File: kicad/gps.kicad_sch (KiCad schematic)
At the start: 4 parts, among them J7 Conn_Coaxial_Small, Q2 IRF540N, U1 NEO-M8N

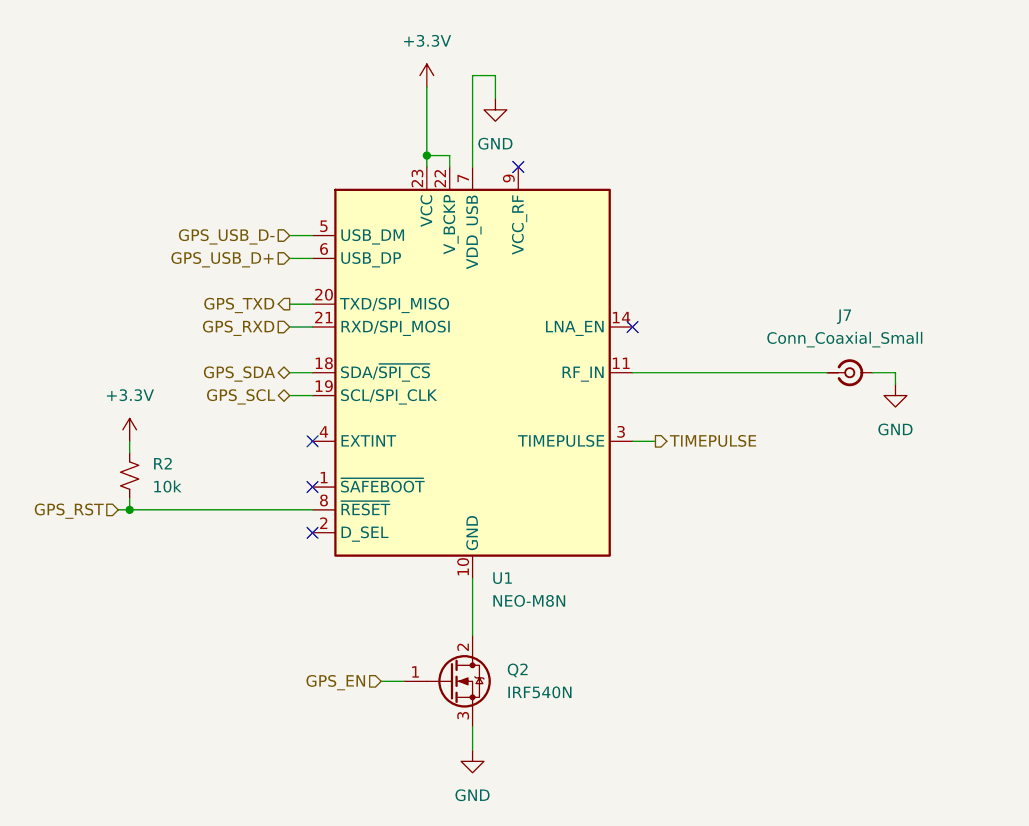
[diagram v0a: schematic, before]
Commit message: make bom cheaper
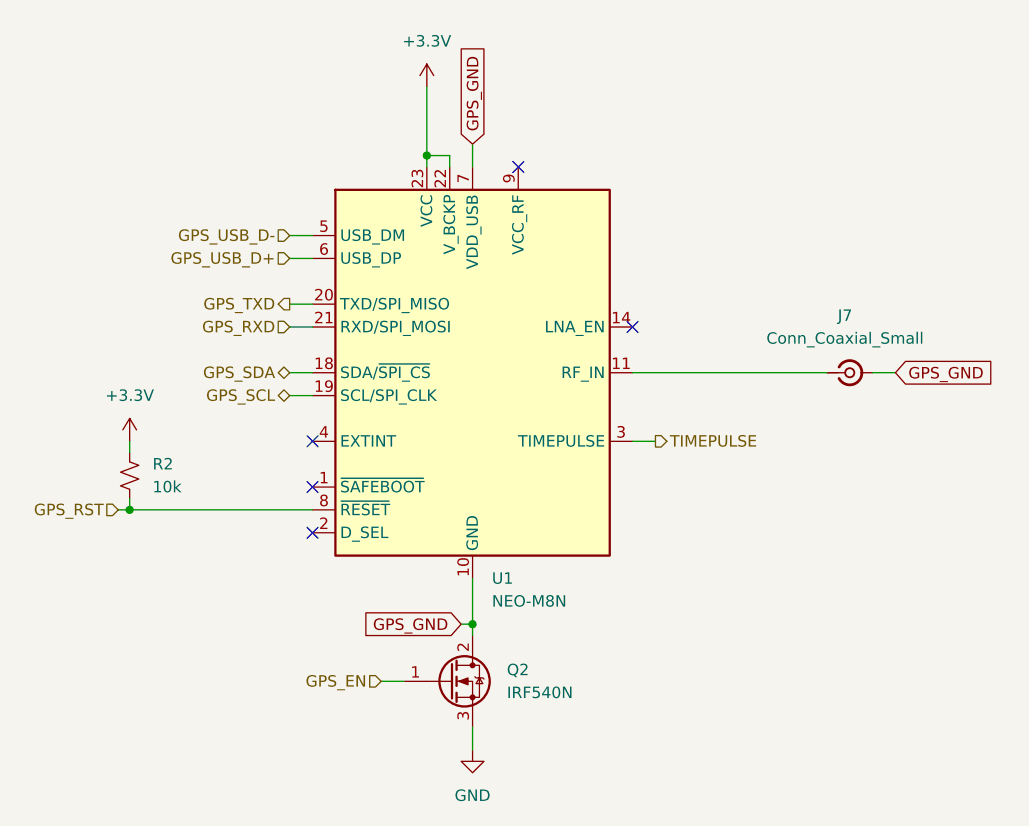
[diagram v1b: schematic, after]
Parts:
- R2: footprint Resistor_THT:R_Axial_DIN0207_L6.3mm_D2.5mm_P10.16mm_Horizontal -> Resistor_THT:R_Axial_DIN0204_L3.6mm_D1.6mm_P2.54mm_Vertical
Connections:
- net GND: no longer J7.2 (Ext), U1.7 (VDD_USB)
- net GPS_GND: now reaches Q2.2 (D), U1.10 (GND), U1.12 (GND), U1.13 (GND), U1.24 (GND)
- net GPS_GND: now also J7.2 (Ext), U1.7 (VDD_USB)
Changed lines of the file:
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@@
+		(color 0 0 0 0)
+	)
+	(junction
+		(at 118.11 124.46)
+		(diameter 0)
 		(color 0 0 0 0)
 	)
@@
 	(wire
 		(pts
+			(xy 118.11 124.46) (xy 118.11 125.73)
+		)
+		(stroke
+			(width 0)
+			(type default)
+		)
+	)
+	(wire
+		(pts
 			(xy 97.79 81.28) (xy 100.33 81.28)
 		)
@@
 	(wire
 		(pts
-			(xy 118.11 119.38) (xy 118.11 125.73)
-		)
-		(stroke
-			(width 0)
-			(type default)
-		)
-	)
-	(wire
-		(pts
 			(xy 78.74 111.76) (xy 80.01 111.76)
 		)
@@
 	(wire
 		(pts
-			(xy 118.11 63.5) (xy 120.65 63.5)
+			(xy 116.84 124.46) (xy 118.11 124.46)
 		)
 		(stroke
@@
 	(wire
 		(pts
-			(xy 118.11 73.66) (xy 118.11 63.5)
-		)
-		(stroke
-			(width 0)
-			(type default)
-		)
-	)
-	(wire
-		(pts
 			(xy 97.79 91.44) (xy 100.33 91.44)
 		)
@@
 	(wire
 		(pts
+			(xy 118.11 119.38) (xy 118.11 124.46)
+		)
+		(stroke
+			(width 0)
+			(type default)
+		)
+	)
+	(wire
+		(pts
 			(xy 113.03 72.39) (xy 113.03 73.66)
 		)
@@
 	(wire
 		(pts
-			(xy 120.65 63.5) (xy 120.65 66.04)
+			(xy 118.11 71.12) (xy 118.11 73.66)
 		)
 		(stroke
@@
 		)
 	)
-	(wire
-		(pts
-			(xy 165.1 97.79) (xy 165.1 96.52)
-		)
-		(stroke
-			(width 0)
-			(type default)
+	(global_label "GPS_GND"
+		(shape input)
+		(at 118.11 71.12 90)
+		(fields_autoplaced yes)
+		(effects
+			(font
+				(size 1.27 1.27)
+			)
+			(justify left)
+		)
+		(property "Intersheetrefs" "${INTERSHEET_REFS}"
+			(at 118.11 59.5472 90)
+			(effects
+				(font
+					(size 1.27 1.27)
+				)
+				(justify left)
+				(hide yes)
+			)
+		)
+	)
+	(global_label "GPS_GND"
+		(shape input)
+		(at 116.84 124.46 180)
+		(fields_autoplaced yes)
+		(effects
+			(font
+				(size 1.27 1.27)
+			)
+			(justify right)
+		)
+		(property "Intersheetrefs" "${INTERSHEET_REFS}"
+			(at 105.2672 124.46 0)
+			(effects
+				(font
+					(size 1.27 1.27)
+				)
+				(justify right)
+				(hide yes)
+			)
+		)
+	)
+	(global_label "GPS_GND"
+		(shape input)
+		(at 165.1 96.52 0)
+		(fields_autoplaced yes)
+		(effects
+			(font
+				(size 1.27 1.27)
+			)
+			(justify left)
+		)
+		(property "Intersheetrefs" "${INTERSHEET_REFS}"
+			(at 176.6728 96.52 0)
+			(effects
+				(font
+					(size 1.27 1.27)
+				)
+				(justify left)
+				(hide yes)
+			)
 		)
 	)
@@
 			)
 		)
-		(property "Footprint" "Resistor_THT:R_Axial_DIN0207_L6.3mm_D2.5mm_P10.16mm_Horizontal"
+		(property "Footprint" "Resistor_THT:R_Axial_DIN0204_L3.6mm_D1.6mm_P2.54mm_Vertical"
 			(at 80.01 107.95 0)
 			(effects
@@
 					(unit 1)
 				)
-			)
-		)
-	)
-	(symbol
-		(lib_id "power:GND")
-		(at 120.65 66.04 0)
-		(unit 1)
-		(exclude_from_sim no)
-		(in_bom yes)
-		(on_board yes)
-		(dnp no)
-		(fields_autoplaced yes)
-		(property "Reference" "#PWR037"
-			(at 120.65 72.39 0)
-			(effects
-				(font
-					(size 1.27 1.27)
-				)
-				(hide yes)
-			)
-		)
-		(property "Value" "GND"
-			(at 120.65 71.12 0)
-			(effects
-				(font
-					(size 1.27 1.27)
-				)
-			)
-		)
-		(property "Footprint" ""
-			(at 120.65 66.04 0)
-			(effects
-				(font
-					(size 1.27 1.27)
-				)
-				(hide yes)
-			)
-		)
-		(property "Datasheet" ""
-			(at 120.65 66.04 0)
-			(effects
-				(font
-					(size 1.27 1.27)
-				)
-				(hide yes)
-			)
-		)
-		(property "Description" "Power symbol creates a global label with name \"GND\" , ground"
-			(at 120.65 66.04 0)
-			(effects
-				(font
-					(size 1.27 1.27)
-				)
-				(hide yes)
-			)
-		)
-		(pin "1"
-		)
-		(instances
-			(project ""
-				(path "/78341cab-a048-4351-a366-4c432cce3019/ff5567d7-137e-4eab-96d1-6f2a00cbcd45"
-					(reference "#PWR037")
-					(unit 1)
-				)
-			)
-		)
-	)
-	(symbol
-		(lib_id "power:GND")
-		(at 165.1 97.79 0)
-		(unit 1)
-		(exclude_from_sim no)
-		(in_bom yes)
-		(on_board yes)
-		(dnp no)
-		(fields_autoplaced yes)
-		(property "Reference" "#PWR038"
-			(at 165.1 104.14 0)
-			(effects
-				(font
-					(size 1.27 1.27)
-				)
-				(hide yes)
-			)
-		)
-		(property "Value" "GND"
-			(at 165.1 102.87 0)
-			(effects
-				(font
-					(size 1.27 1.27)
-				)
-			)
-		)
-		(property "Footprint" ""
-			(at 165.1 97.79 0)
-			(effects
-				(font
-					(size 1.27 1.27)
-				)
-				(hide yes)
-			)
-		)
-		(property "Datasheet" ""
-			(at 165.1 97.79 0)
-			(effects
-				(font
-					(size 1.27 1.27)
-				)
-				(hide yes)
-			)
-		)
-		(property "Description" "Power symbol creates a global label with name \"GND\" , ground"
-			(at 165.1 97.79 0)
-			(effects
-				(font
-					(size 1.27 1.27)
-				)
-				(hide yes)
-			)
-		)
-		(pin "1"
-		)
-		(instances
-			(project ""
-				(path "/78341cab-a048-4351-a366-4c432cce3019/ff5567d7-137e-4eab-96d1-6f2a00cbcd45"
-					(reference "#PWR038")
-					(unit 1)
-				)

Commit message: updadte
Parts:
- added C11: 100nF, Capacitor_THT:C_Disc_D5.0mm_W2.5mm_P5.00mm, symbol Device:C
- added C12: 10uF, Capacitor_THT:CP_Radial_D5.0mm_P2.50mm, symbol Device:C_Polarized_US
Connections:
- net +3.3V: now also C11.1, C12.1
- net GND: now also C11.2, C12.2
